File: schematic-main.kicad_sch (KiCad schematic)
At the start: 7 parts, among them J1 Battery, J2 CAN, P1 USB_C_Plug_USB2.0

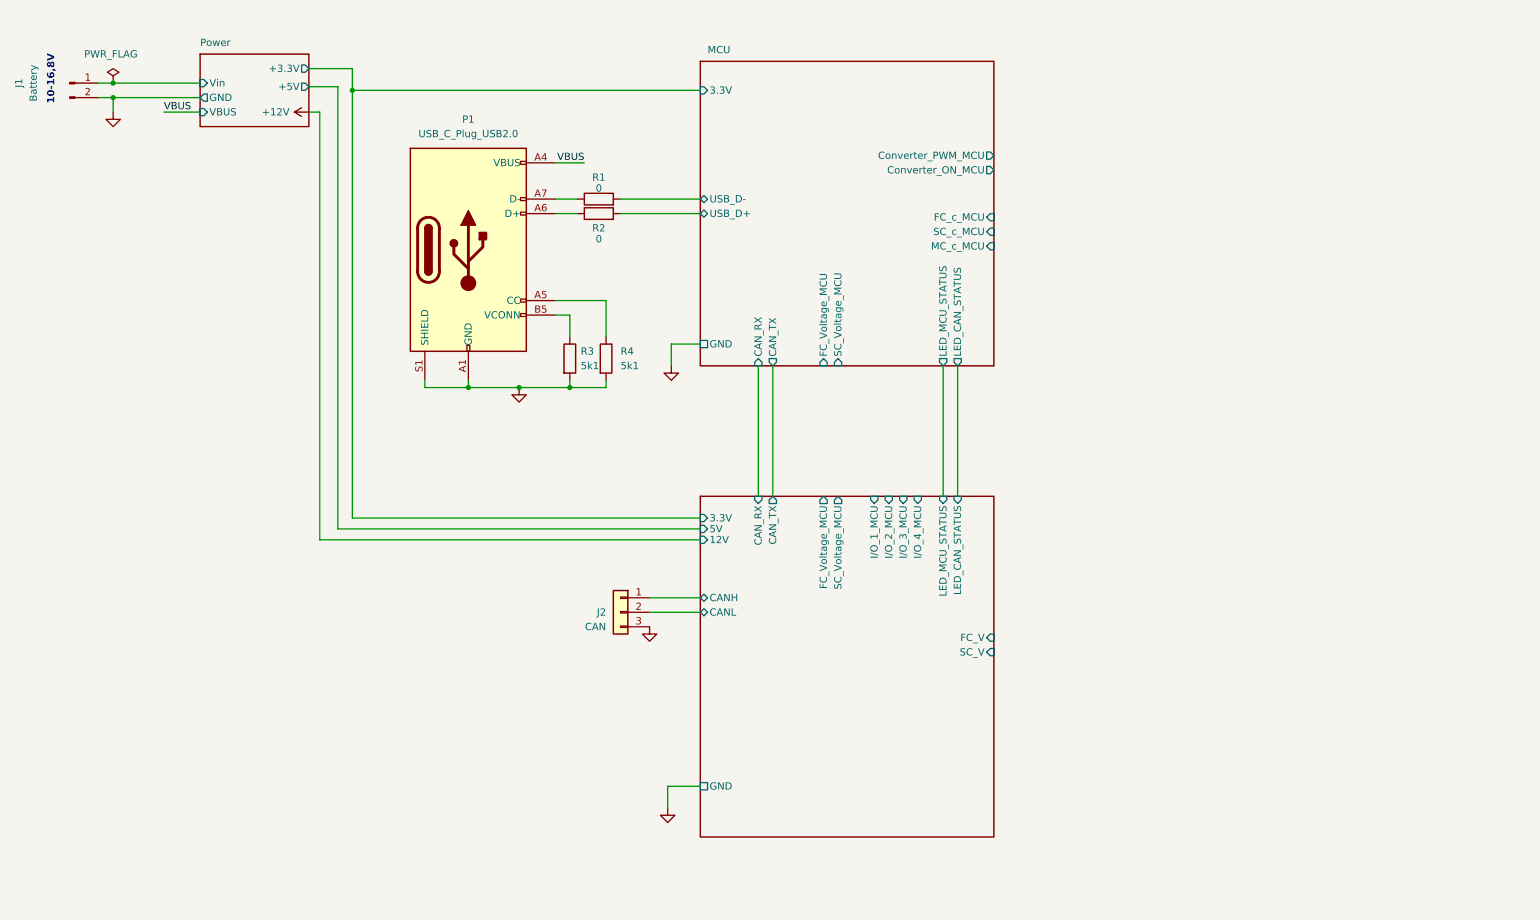
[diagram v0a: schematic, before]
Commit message: Add footprints, Placing MCU
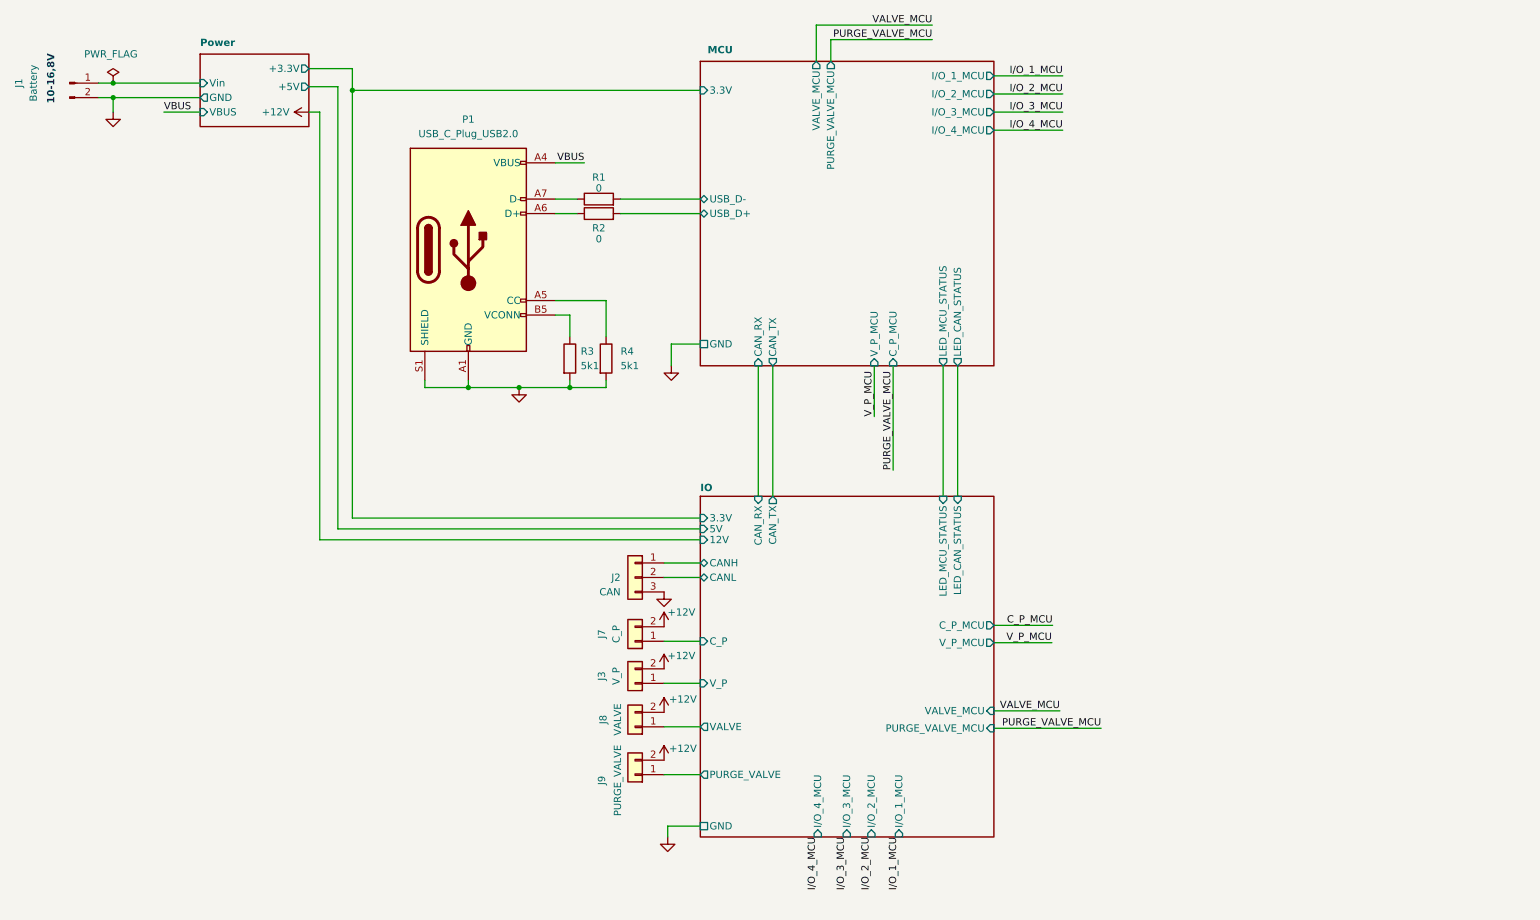
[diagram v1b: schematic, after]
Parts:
- added J3: V_P, Connector_Molex:39-30-102Y, symbol Connector_Generic:Conn_01x02
- added J7: C_P, Connector_Molex:39-30-102Y, symbol Connector_Generic:Conn_01x02
- added J8: VALVE, Connector_Molex:39-30-102Y, symbol Connector_Generic:Conn_01x02
- added J9: PURGE_VALVE, Connector_Molex:39-30-102Y, symbol Connector_Generic:Conn_01x02
- J2: footprint Connector_Molex:Molex_Mini-Fit_Jr_5569-02A2_2x01_P4.20mm_Horizontal -> Connector_Molex:39303035
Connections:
- net +12V: now also J3.2 (Pin_2), J7.2 (Pin_2), J8.2 (Pin_2), J9.2 (Pin_2)
- new net IO/C_P: J7.1 (Pin_1)
- new net IO/PURGE_VALVE: J9.1 (Pin_1)
- new net IO/VALVE: J8.1 (Pin_1)
- new net IO/V_P: J3.1 (Pin_1)
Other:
- sheet IO ports: added C_P, C_P_MCU, PURGE_VALVE, PURGE_VALVE_MCU, VALVE, VALVE_MCU, V_P, V_P_MCU; removed FC_V, FC_Voltage_MCU, SC_V, SC_Voltage_MCU
- sheet MCU ports: added C_P_MCU, I/O_1_MCU, I/O_2_MCU, I/O_3_MCU, I/O_4_MCU, PURGE_VALVE_MCU, VALVE_MCU, V_P_MCU; removed Converter_ON_MCU, Converter_PWM_MCU, FC_Voltage_MCU, FC_c_MCU, MC_c_MCU, SC_Voltage_MCU, SC_c_MCU
- moved on the sheet: J2

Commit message: Drawing PCB
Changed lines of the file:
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@@
+    (stroke (width 0) (type default))
+  )
+  (wire (pts (xy 168.402 81.28) (xy 168.402 90.17))
     (stroke (width 0) (type default))
   )
@@
   )
   (wire (pts (xy 165.1 81.28) (xy 165.1 90.17))
-    (stroke (width 0) (type default))
-  )
-  (wire (pts (xy 168.402 81.28) (xy 168.402 99.568))
     (stroke (width 0) (type default))
   )
@@
     (effects (font (size 1.27 1.27)) (justify right bottom))
   )
+  (label "C_P_MCU" (at 168.402 90.17 90) (fields_autoplaced)
+    (effects (font (size 1.27 1.27)) (justify left bottom))
+  )
   (label "V_P_MCU" (at 196.215 129.794 180) (fields_autoplaced)
     (effects (font (size 1.27 1.27)) (justify right bottom))
@@
     (effects (font (size 1.27 1.27)) (justify left bottom))
   )
-  (label "PURGE_VALVE_MCU" (at 168.402 99.568 90) (fields_autoplaced)
-    (effects (font (size 1.27 1.27)) (justify left bottom))
-  )

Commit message: Makin GND sphere
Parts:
- added H1, H2, H3, H4: MountingHole, MountingHole:MountingHole_3.2mm_M3_DIN965, symbol Mechanical:MountingHole
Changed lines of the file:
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@@
     (stroke (width 0) (type default))
+  )
+  (rectangle (start 27.94 126.746) (end 53.34 154.686)
+    (stroke (width 0) (type dash))
+    (fill (type none))
   )
   (text "10-16,8V" (at 21.59 35.56 90)
@@
     )
   )
+  (symbol (lib_id "Mechanical:MountingHole") (at 34.29 137.668 0) (unit 1)
+    (in_bom yes) (on_board yes) (dnp no) (fields_autoplaced)
+    (property "Reference" "H2" (at 36.83 136.398 0)
+      (effects (font (size 1.27 1.27)) (justify left))
+    )
+    (property "Value" "MountingHole" (at 36.83 138.938 0)
+      (effects (font (size 1.27 1.27)) (justify left))
+    )
+    (property "Footprint" "MountingHole:MountingHole_3.2mm_M3_DIN965" (at 34.29 137.668 0)
+      (effects (font (size 1.27 1.27)) hide)
+    )
+    (property "Datasheet" "~" (at 34.29 137.668 0)
+      (effects (font (size 1.27 1.27)) hide)
+    )
+    (instances
+      (project "schematic-main"
+        (path "/c9ad7189-d3b2-414a-9743-efd8e57cd755"
+          (reference "H2") (unit 1)
+        )
+      )
+    )
+  )
   (symbol (lib_id "Connector:Conn_01x02_Pin") (at 24.13 31.75 0) (unit 1)
     (in_bom yes) (on_board yes) (dnp no)
@@
         (path "/c9ad7189-d3b2-414a-9743-efd8e57cd755"
           (reference "#PWR01") (unit 1)
+        )
+      )
+    )
+  )
+  (symbol (lib_id "Mechanical:MountingHole") (at 34.29 149.479 0) (unit 1)
+    (in_bom yes) (on_board yes) (dnp no) (fields_autoplaced)
+    (property "Reference" "H4" (at 36.83 148.209 0)
+      (effects (font (size 1.27 1.27)) (justify left))
+    )
+    (property "Value" "MountingHole" (at 36.83 150.749 0)
+      (effects (font (size 1.27 1.27)) (justify left))
+    )
+    (property "Footprint" "MountingHole:MountingHole_3.2mm_M3_DIN965" (at 34.29 149.479 0)
+      (effects (font (size 1.27 1.27)) hide)
+    )
+    (property "Datasheet" "~" (at 34.29 149.479 0)
+      (effects (font (size 1.27 1.27)) hide)
+    )
+    (instances
+      (project "schematic-main"
+        (path "/c9ad7189-d3b2-414a-9743-efd8e57cd755"
+          (reference "H4") (unit 1)
         )
       )
@@
     )
   )
+  (symbol (lib_id "Mechanical:MountingHole") (at 34.29 131.699 0) (unit 1)
+    (in_bom yes) (on_board yes) (dnp no) (fields_autoplaced)
+    (property "Reference" "H1" (at 36.83 130.429 0)
+      (effects (font (size 1.27 1.27)) (justify left))
+    )
+    (property "Value" "MountingHole" (at 36.83 132.969 0)
+      (effects (font (size 1.27 1.27)) (justify left))
+    )
+    (property "Footprint" "MountingHole:MountingHole_3.2mm_M3_DIN965" (at 34.29 131.699 0)
+      (effects (font (size 1.27 1.27)) hide)
+    )
+    (property "Datasheet" "~" (at 34.29 131.699 0)
+      (effects (font (size 1.27 1.27)) hide)
+    )
+    (instances
+      (project "schematic-main"
+        (path "/c9ad7189-d3b2-414a-9743-efd8e57cd755"
+          (reference "H1") (unit 1)
+        )
+      )
+    )
+  )
   (symbol (lib_id "power:+12V") (at 128.27 150.368 0) (unit 1)
     (in_bom yes) (on_board yes) (dnp no)
@@
         )
       )
+    )
+  )
+  (symbol (lib_id "Mechanical:MountingHole") (at 34.29 143.637 0) (unit 1)
+    (in_bom yes) (on_board yes) (dnp no) (fields_autoplaced)
+    (property "Reference" "H3" (at 36.83 142.367 0)
+      (effects (font (size 1.27 1.27)) (justify left))
+    )
+    (property "Value" "MountingHole" (at 36.83 144.907 0)
+      (effects (font (size 1.27 1.27)) (justify left))
+    )
+    (property "Footprint" "MountingHole:MountingHole_3.2mm_M3_DIN965" (at 34.29 143.637 0)
+      (effects (font (size 1.27 1.27)) hide)
+    )
+    (property "Datasheet" "~" (at 34.29 143.637 0)
+      (effects (font (size 1.27 1.27)) hide)
+    )
+    (instances
+      (project "schematic-main"
+        (path "/c9ad7189-d3b2-414a-9743-efd8e57cd755"
+          (reference "H3") (unit 1)
+        )
+      )

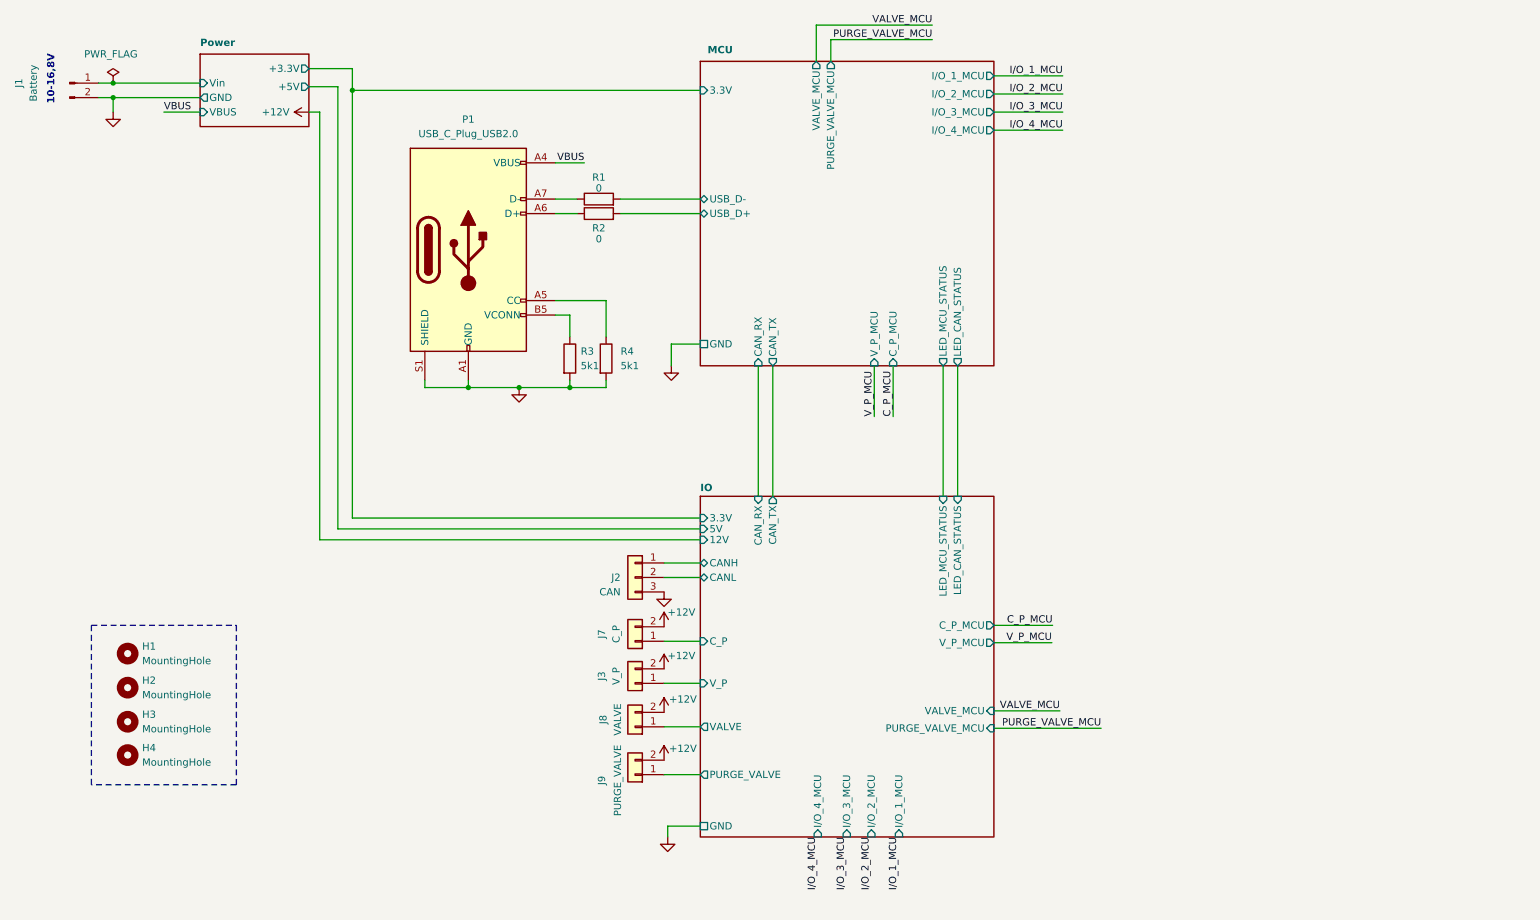
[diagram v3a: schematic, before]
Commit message: Adding connector for Hydrogen Sensor
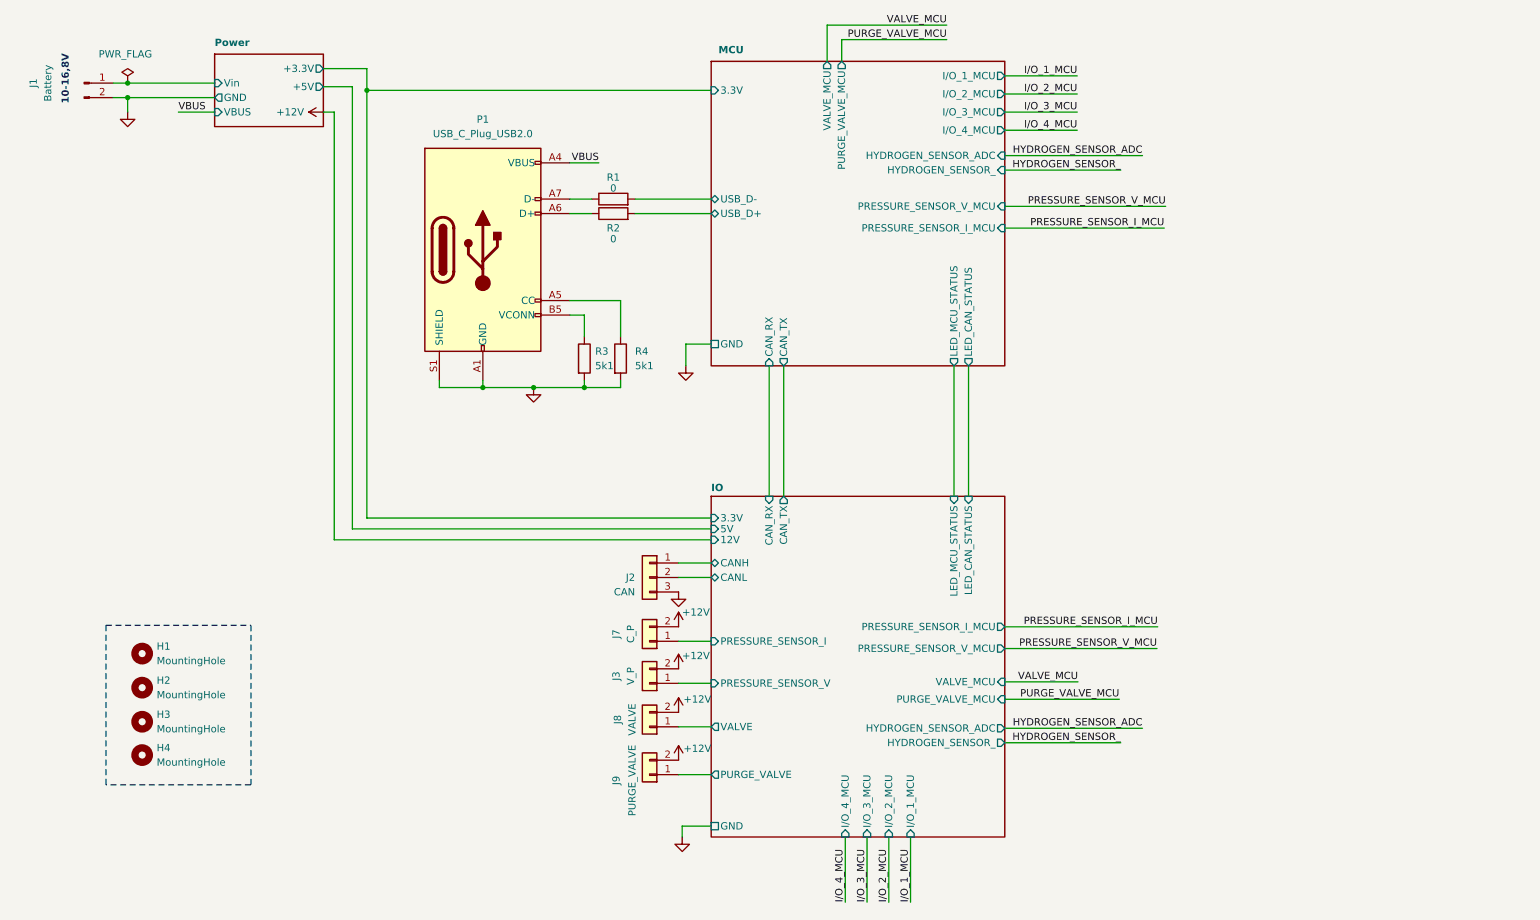
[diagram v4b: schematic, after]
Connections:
- net IO/C_P renamed IO/PRESSURE_SENSOR_I
- net IO/V_P renamed IO/PRESSURE_SENSOR_V
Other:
- sheet IO ports: added HYDROGEN_SENSOR_, HYDROGEN_SENSOR_ADC, PRESSURE_SENSOR_I, PRESSURE_SENSOR_I_MCU, PRESSURE_SENSOR_V, PRESSURE_SENSOR_V_MCU; removed C_P, C_P_MCU, V_P, V_P_MCU
- sheet MCU ports: added HYDROGEN_SENSOR_, HYDROGEN_SENSOR_ADC, PRESSURE_SENSOR_I_MCU, PRESSURE_SENSOR_V_MCU; removed C_P_MCU, V_P_MCU
- moved on the sheet: H1, H2, H3, H4, J1, J2, J3, J7, J8, J9, P1, R1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

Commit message: Adding motor driver unit
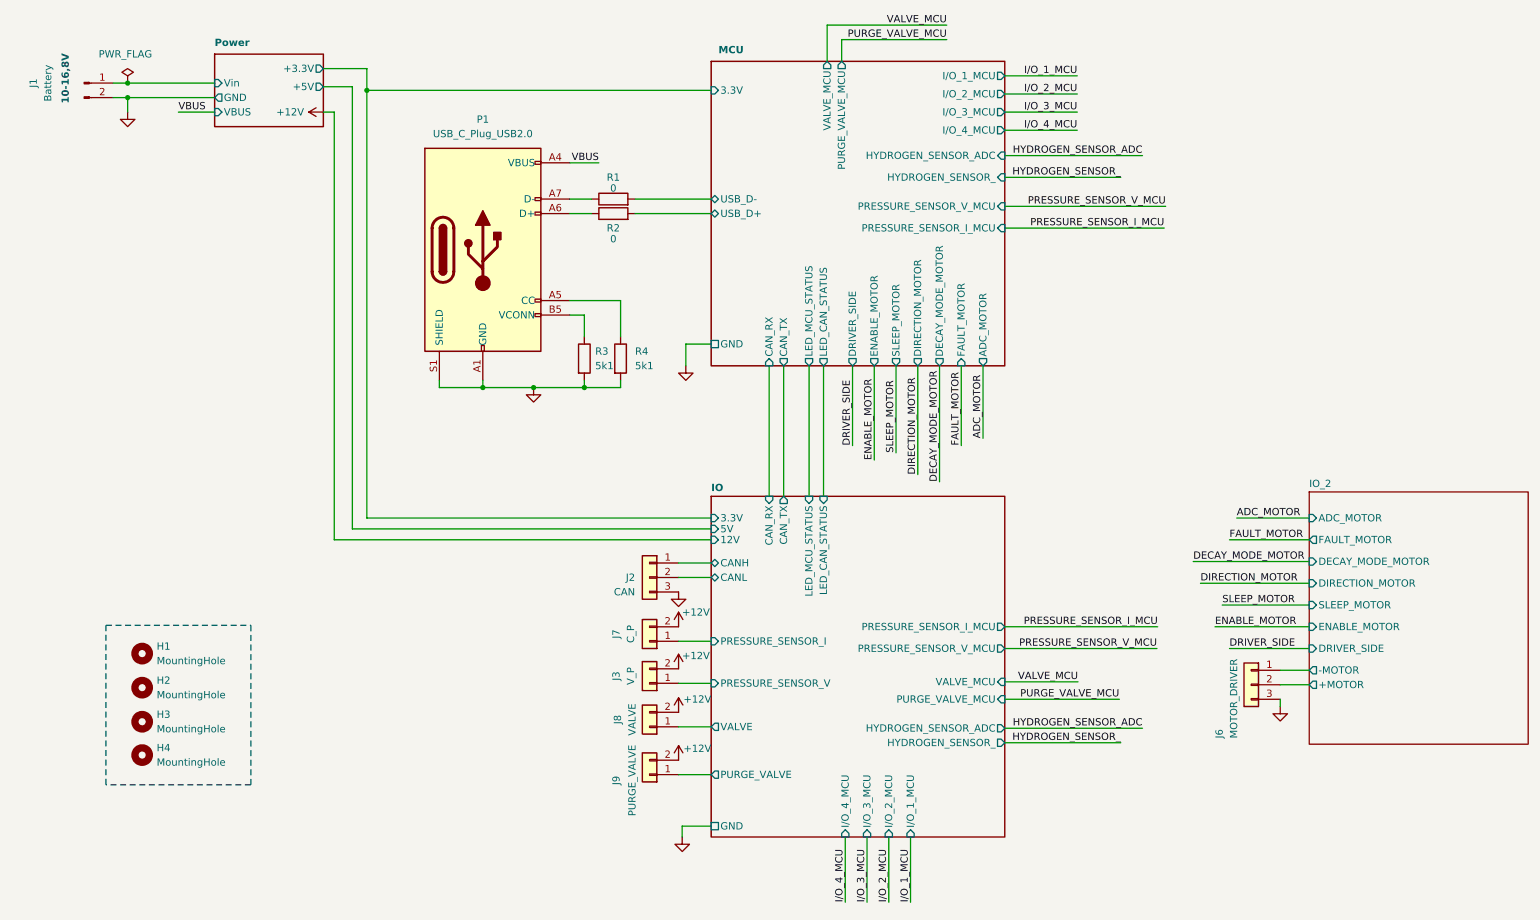
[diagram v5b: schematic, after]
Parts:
- added J6: MOTOR_DRIVER, Connector_Molex:Molex_KK-396_A-41792-0003_1x03_P3.96mm_Horizontal, symbol Connector_Generic:Conn_01x03
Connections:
- net GND: now also J6.3 (Pin_3)
- new net IO_2/+MOTOR: J6.2 (Pin_2)
- new net IO_2/-MOTOR: J6.1 (Pin_1)
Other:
- added sheet IO_2 (untitled.kicad_sch)
- sheet MCU ports: added ADC_MOTOR, DECAY_MODE_MOTOR, DIRECTION_MOTOR, DRIVER_SIDE, ENABLE_MOTOR, FAULT_MOTOR, SLEEP_MOTOR; removed none
